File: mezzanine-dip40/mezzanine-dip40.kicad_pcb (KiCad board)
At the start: 4 copper layers, 19 x 52.1 mm, 3 parts, among them J1 Conn_01x20, J2 Conn_01x20

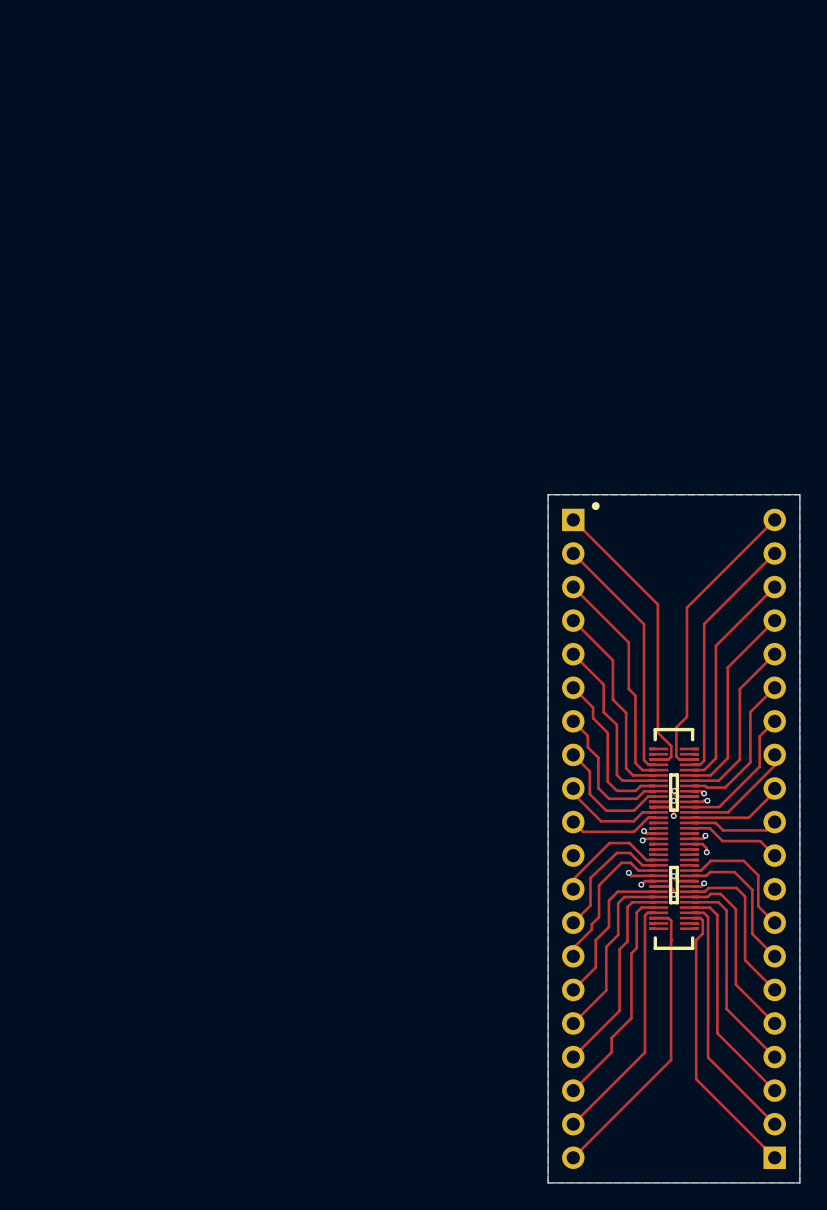
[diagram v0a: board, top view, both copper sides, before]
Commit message: Update mezzanine and Z80 QFN hardware designs
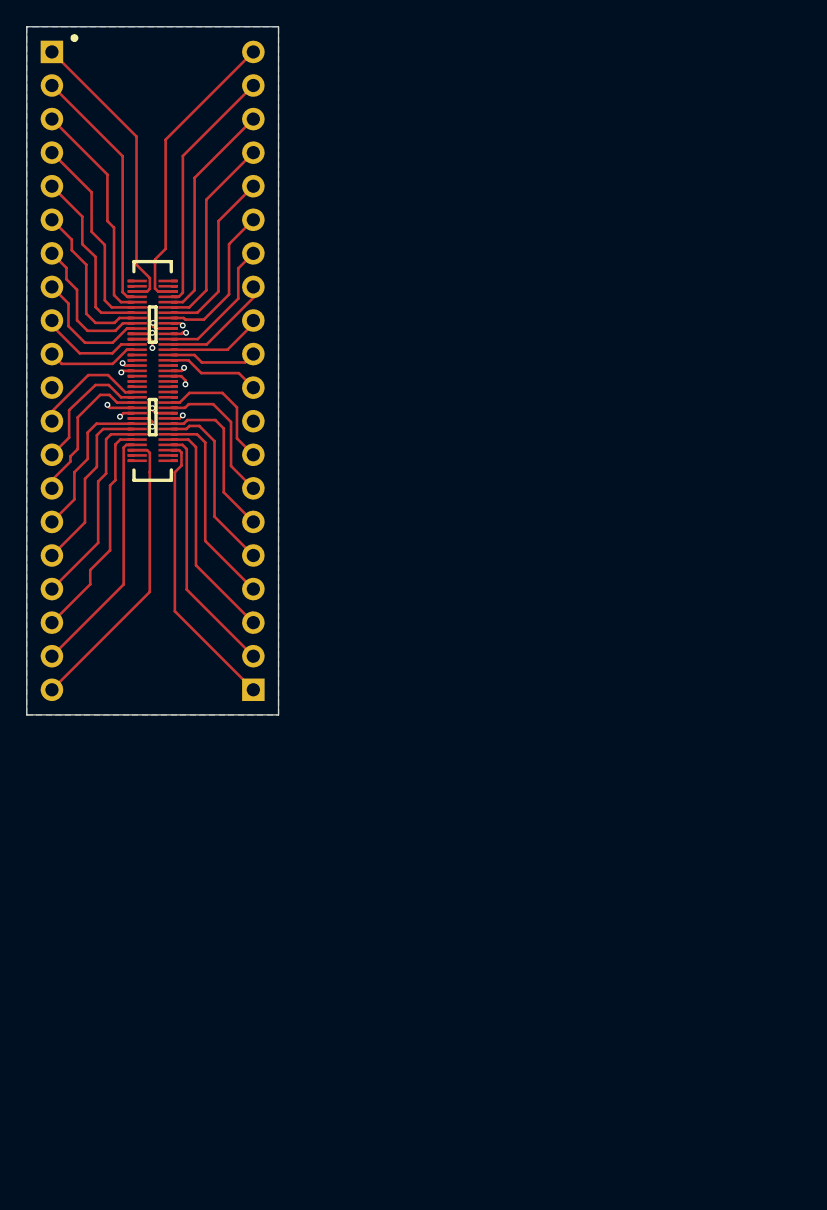
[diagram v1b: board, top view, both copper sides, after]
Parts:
- moved J2 53.0 mm to (111.2, 110.1)
- moved U2 53.0 mm to (103.6, 86.0)
- moved J1 53.0 mm to (95.9, 61.9)
